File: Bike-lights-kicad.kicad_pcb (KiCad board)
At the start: 2 copper layers, 49 parts, among them J1 tag-connect-swd, Q1 2N7002, Q2 2N7002, Q3 2N7002, Q4 2N7002, Q5 2N7002, SW1 SW_Push, U1 ADP2108AUJ-1.8, U2 MC34673, U3 DIO6605B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

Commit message: output ready
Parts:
- removed R1: 100K, Resistor_SMD:R_0603_1608Metric
- added REF**: MountingHole_3mm, MountingHole:MountingHole_3mm, F.Cu at (52.5, 7.85)
- added REF**: MountingHole_3mm, MountingHole:MountingHole_3mm, F.Cu at (16.5, 7.85)
- added REF**: MountingHole_2.2mm_M2_ISO14580_Pad, MountingHole:MountingHole_2.2mm_M2_ISO14580_Pad, F.Cu at (40.5, 7.85)
- J1, TP1, TP2, TP3, TP4: moved to B.Cu
- moved C9 174.9 mm to (3.60, 2.40)
- moved R4 165.7 mm to (3.60, 13.3)
- moved R8 163.3 mm to (9.70, 11.1)
- moved R9 159.6 mm to (21.7, 11.1)
- moved TP4 153.9 mm to (3.47, 10.5), turned to 90 degrees
- moved Q1 152.3 mm to (10.1, 13.6), turned to 180 degrees
- moved TP3 152.2 mm to (3.47, 5.40), turned to -90 degrees
- moved D1 149.7 mm to (10.5, 9.12), turned to 90 degrees
- moved R10 146.3 mm to (33.7, 11.1)
- moved Q2 144.8 mm to (22.1, 13.6), turned to 180 degrees
- moved SW1 142.1 mm to (3.50, 7.85), turned to 90 degrees
- moved D2 137.9 mm to (22.5, 9.12), turned to 90 degrees
- moved Q3 134.6 mm to (34.1, 13.6), turned to 180 degrees
- moved R11 132.8 mm to (45.7, 11.1)
- moved R12 129.9 mm to (57.7, 11.1)
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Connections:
- C7 pad 1: /VBATT -> /VBAT
- TP1 pad 1: /VBATT -> /VBAT
- U2 pad 4: Net-(R1-Pad1) -> /PM_CHG_5V_INPUT
- U3 pad 7: (no net) -> +5V
- U3 pad 8: +5V -> unconnected-(U3-Pad8)
- U5 pad 2: /VBATT -> /VBAT
- U5 pad 3: /VBATT -> /VBAT
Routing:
- net +1V8: track 0.00 -> 151.0 mm, vias 0 -> 5
- net /PM_CHG_5V_INPUT: track 0.00 -> 108.7 mm, vias 0 -> 6
- net +5V: track 0.00 -> 103.1 mm, vias 0 -> 1
- net /TUBE_BTN: track 0.00 -> 83.2 mm, vias 0 -> 2
- net /D_EN0: track 0.00 -> 64.1 mm, vias 0 -> 2
- net /D_EN1: track 0.00 -> 53.0 mm, vias 0 -> 2
- net /FUEL_INT: track 0.00 -> 47.1 mm, vias 0 -> 2
- net /I2C1_SCL: track 0.00 -> 46.1 mm, vias 0 -> 4
- net /VBAT: track 0.00 -> 45.5 mm, vias 0 -> 5
- net /I2C1_SDA: track 0.00 -> 44.5 mm, vias 0 -> 2
- net /D_EN2: track 0.00 -> 41.8 mm, vias 0 -> 2
- net GND: track 0.00 -> 34.9 mm, vias 0 -> 44
- net /D_EN3: track 0.00 -> 30.5 mm, vias 0 -> 2
- net /ACC_INT1: track 0.00 -> 29.1 mm
- net /D_EN4: track 0.00 -> 25.6 mm
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- added copper zone on B.Cu, net GND
- added copper zone on F.Cu, net GND
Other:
- board outline added: 105.9 x 15.7 mm
- board text added: "5V"
- board text added: "BAT+"
- board text added: "BAT-"
- board text added: "CHG INPUT"
- board text added: "GND"
- board text added: "TO BATTERY max 1A charge"
- board text added: "bikelight rev B Alexis Marquet"

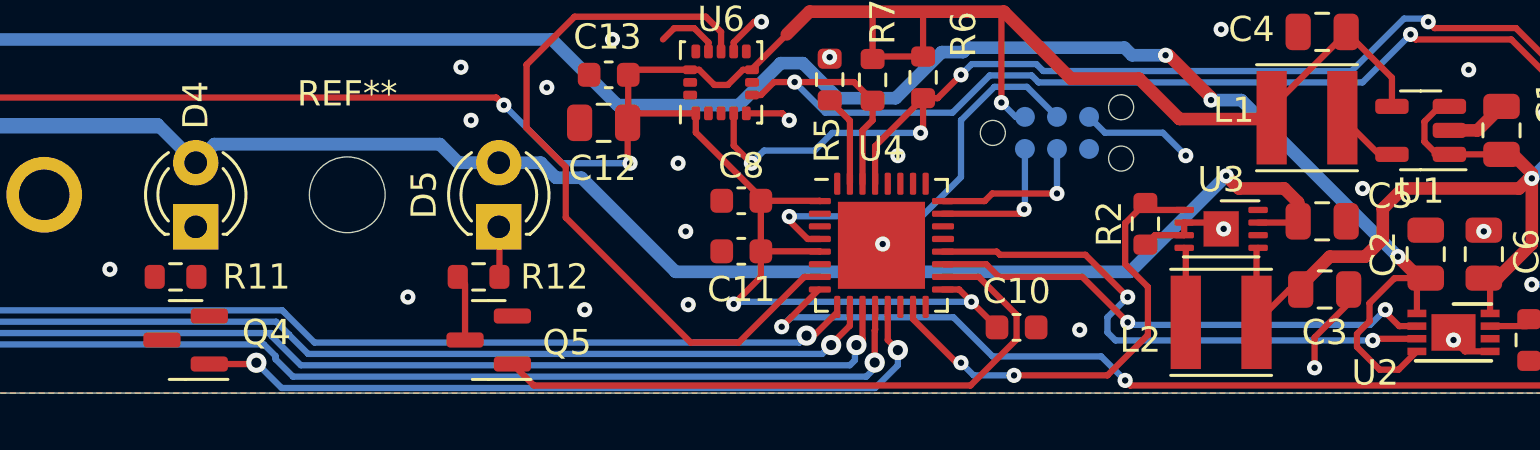
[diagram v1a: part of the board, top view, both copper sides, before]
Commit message: fixed 3 unconnected nets after sending to production...
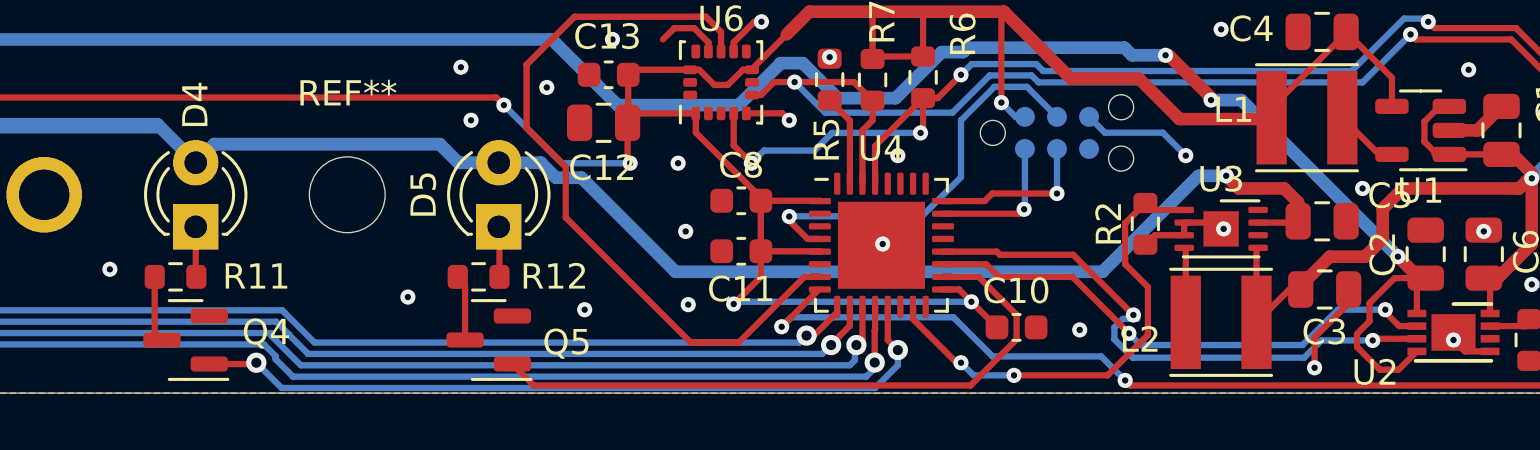
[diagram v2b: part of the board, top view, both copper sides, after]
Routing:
- net Net-(Q4-Pad3): track 0.00 -> 2.62 mm
- net Net-(D4-Pad1): track 0.00 -> 1.99 mm
- net /PM_CHG_CHARGING: track 22.2 -> 22.9 mm
- net /PM_CHG_PRESENT: track 20.3 -> 21.0 mm
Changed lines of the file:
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@@
   (segment (start 88.5625 8.95) (end 90.1 8.95) (width 0.25) (layer "F.Cu") (net 5))
   (via (at 87.3 7.1) (size 0.6) (drill 0.25) (layers "F.Cu" "B.Cu") (net 5))
-  (segment (start 60.166828 6.58) (end 60.761828 7.175) (width 0.5) (layer "B.Cu") (net 5))
+  (segment (start 60.761828 7.175) (end 61.775 7.175) (width 0.5) (layer "B.Cu") (net 5))
   (segment (start 10.5 6.58) (end 12.437062 4.642938) (width 0.508) (layer "B.Cu") (net 5))
   (segment (start 12.437062 4.642938) (end 20.562938 4.642938) (width 0.508) (layer "B.Cu") (net 5))
-  (segment (start 83.5 10.9) (end 87.3 7.1) (width 0.5) (layer "B.Cu") (net 5))
   (segment (start 34.5 6.58) (end 36.016524 5.063476) (width 0.508) (layer "B.Cu") (net 5))
+  (segment (start 82.4 10.9) (end 86.2 7.1) (width 0.5) (layer "B.Cu") (net 5))
   (segment (start 46.5 6.58) (end 47.234001 5.845999) (width 0.508) (layer "B.Cu") (net 5))
   (segment (start 47.234001 5.845999) (end 56.164169 5.845999) (width 0.508) (layer "B.Cu") (net 5))
   (segment (start 34.5 6.58) (end 35.780657 5.299343) (width 0.25) (layer "B.Cu") (net 5))
   (segment (start 61.775 7.175) (end 65.5 10.9) (width 0.5) (layer "B.Cu") (net 5))
-  (segment (start 58.5 6.58) (end 60.166828 6.58) (width 0.5) (layer "B.Cu") (net 5))
+  (segment (start 86.2 7.1) (end 87.3 7.1) (width 0.5) (layer "B.Cu") (net 5))
   (segment (start 46.5 6.58) (end 47.105001 5.974999) (width 0.25) (layer "B.Cu") (net 5))
   (segment (start 45.219343 5.299343) (end 46.5 6.58) (width 0.25) (layer "B.Cu") (net 5))
+  (segment (start 60.166828 6.58) (end 60.761828 7.175) (width 0.5) (layer "B.Cu") (net 5))
   (segment (start 35.780657 5.299343) (end 45.219343 5.299343) (width 0.25) (layer "B.Cu") (net 5))
-  (segment (start 60.761828 7.175) (end 61.775 7.175) (width 0.5) (layer "B.Cu") (net 5))
+  (segment (start 65.5 10.9) (end 82.4 10.9) (width 0.5) (layer "B.Cu") (net 5))
   (segment (start 56.164169 5.845999) (end 56.89817 6.58) (width 0.508) (layer "B.Cu") (net 5))
   (segment (start 56.89817 6.58) (end 58.5 6.58) (width 0.508) (layer "B.Cu") (net 5))
+  (segment (start 58.5 6.58) (end 60.166828 6.58) (width 0.5) (layer "B.Cu") (net 5))
   (segment (start 36.016524 5.063476) (end 44.983476 5.063476) (width 0.508) (layer "B.Cu") (net 5))
-  (segment (start 65.5 10.9) (end 83.5 10.9) (width 0.5) (layer "B.Cu") (net 5))
   (segment (start 20.562938 4.642938) (end 22.5 6.58) (width 0.508) (layer "B.Cu") (net 5))
   (segment (start 22.5 6.58) (end 34.5 6.58) (width 0.508) (layer "B.Cu") (net 5))
@@
   (segment (start 22.525 11.1) (end 22.525 9.145) (width 0.25) (layer "F.Cu") (net 9))
   (segment (start 34.5 9.12) (end 34.5 11.075) (width 0.25) (layer "F.Cu") (net 10))
+  (segment (start 46.5 11.075) (end 46.525 11.1) (width 0.25) (layer "F.Cu") (net 11))
+  (segment (start 46.5 9.12) (end 46.5 11.075) (width 0.25) (layer "F.Cu") (net 11))
   (segment (start 58.525 11.1) (end 58.525 9.145) (width 0.25) (layer "F.Cu") (net 12))
   (segment (start 79.1245 8.6) (end 76.0875 8.6) (width 0.25) (layer "F.Cu") (net 13))
@@
   (segment (start 49.9 15.5) (end 48.9 14.5) (width 0.25) (layer "B.Cu") (net 25))
   (segment (start 74.3 14.6) (end 73.4 15.5) (width 0.25) (layer "B.Cu") (net 25))
+  (segment (start 44.875 13.3125) (end 45.1625 13.6) (width 0.25) (layer "F.Cu") (net 26))
+  (segment (start 44.875 11.1) (end 44.875 13.3125) (width 0.25) (layer "F.Cu") (net 26))
   (segment (start 79 13.577817) (end 79 12.6) (width 0.25) (layer "F.Cu") (net 27))
   (segment (start 77.5 11.1) (end 76.0875 11.1) (width 0.25) (layer "F.Cu") (net 27))
@@
   (segment (start 71.425 4.6) (end 70.2125 3.3875) (width 0.25) (layer "B.Cu") (net 33))
   (segment (start 77.938604 3.125) (end 76.463604 4.6) (width 0.25) (layer "B.Cu") (net 33))
+  (segment (start 77.8 10.6) (end 76.0875 10.6) (width 0.25) (layer "F.Cu") (net 34))
   (segment (start 93.6 12.4) (end 93.6 12.5) (width 0.25) (layer "F.Cu") (net 34))
-  (segment (start 77.8 10.6) (end 76.0875 10.6) (width 0.25) (layer "F.Cu") (net 34))
   (segment (start 93.6 12.5) (end 94.15 13.05) (width 0.25) (layer "F.Cu") (net 34))
   (segment (start 94.15 13.05) (end 94.85 13.05) (width 0.25) (layer "F.Cu") (net 34))
-  (segment (start 83.4 12.9) (end 81.6 11.1) (width 0.25) (layer "F.Cu") (net 34))
-  (segment (start 81.6 11.1) (end 78.3 11.1) (width 0.25) (layer "F.Cu") (net 34))
+  (segment (start 81.212466 11.1) (end 78.3 11.1) (width 0.25) (layer "F.Cu") (net 34))
+  (segment (start 83.45 13.337534) (end 81.212466 11.1) (width 0.25) (layer "F.Cu") (net 34))
   (segment (start 78.3 11.1) (end 77.8 10.6) (width 0.25) (layer "F.Cu") (net 34))
   (via (at 93.6 12.4) (size 0.6) (drill 0.25) (layers "F.Cu" "B.Cu") (net 34))
-  (via (at 83.4 12.9) (size 0.6) (drill 0.25) (layers "F.Cu" "B.Cu") (net 34))
-  (segment (start 93 13) (end 93.6 12.4) (width 0.25) (layer "B.Cu") (net 34))
-  (segment (start 83.5 13) (end 93 13) (width 0.25) (layer "B.Cu") (net 34))
-  (segment (start 83.4 12.9) (end 83.5 13) (width 0.25) (layer "B.Cu") (net 34))
-  (segment (start 81.725 10.225) (end 78.341116 10.225) (width 0.25) (layer "F.Cu") (net 35))
+  (via (at 83.45 13.337534) (size 0.6) (drill 0.25) (layers "F.Cu" "B.Cu") (net 34))
+  (segment (start 91.721141 12.4) (end 93.6 12.4) (width 0.25) (layer "B.Cu") (net 34))
+  (segment (start 83.45 13.337534) (end 83.912466 13.8) (width 0.25) (layer "B.Cu") (net 34))
+  (segment (start 90.321141 13.8) (end 91.721141 12.4) (width 0.25) (layer "B.Cu") (net 34))
+  (segment (start 83.912466 13.8) (end 90.321141 13.8) (width 0.25) (layer "B.Cu") (net 34))
   (segment (start 78.341116 10.225) (end 78.216116 10.1) (width 0.25) (layer "F.Cu") (net 35))
+  (segment (start 78.216116 10.1) (end 76.0875 10.1) (width 0.25) (layer "F.Cu") (net 35))
+  (segment (start 83.6255 12.608868) (end 81.241632 10.225) (width 0.25) (layer "F.Cu") (net 35))
   (segment (start 93.168671 13.55) (end 93.102667 13.616004) (width 0.25) (layer "F.Cu") (net 35))
-  (segment (start 83.4 11.9) (end 81.725 10.225) (width 0.25) (layer "F.Cu") (net 35))
   (segment (start 94.85 13.55) (end 93.168671 13.55) (width 0.25) (layer "F.Cu") (net 35))
-  (segment (start 78.216116 10.1) (end 76.0875 10.1) (width 0.25) (layer "F.Cu") (net 35))
-  (via (at 83.4 11.9) (size 0.6) (drill 0.25) (layers "F.Cu" "B.Cu") (net 35))
+  (segment (start 81.241632 10.225) (end 78.341116 10.225) (width 0.25) (layer "F.Cu") (net 35))
+  (via (at 83.6255 12.608868) (size 0.6) (drill 0.25) (layers "F.Cu" "B.Cu") (net 35))
   (via (at 93.102667 13.616004) (size 0.6) (drill 0.25) (layers "F.Cu" "B.Cu") (net 35))
-  (segment (start 82.6 13.3) (end 82.916004 13.616004) (width 0.25) (layer "B.Cu") (net 35))
-  (segment (start 82.6 12.7) (end 82.6 13.3) (width 0.25) (layer "B.Cu") (net 35))
-  (segment (start 82.916004 13.616004) (end 93.102667 13.616004) (width 0.25) (layer "B.Cu") (net 35))
-  (segment (start 83.4 11.9) (end 82.6 12.7) (width 0.25) (layer "B.Cu") (net 35))
+  (segment (start 82.875 13.099361) (end 82.875 13.575707) (width 0.25) (layer "B.Cu") (net 35))
+  (segment (start 83.211827 12.762534) (end 82.875 13.099361) (width 0.25) (layer "B.Cu") (net 35))
+  (segment (start 91.070823 13.616004) (end 93.102667 13.616004) (width 0.25) (layer "B.Cu") (net 35))
+  (segment (start 83.599293 14.3) (end 90.386827 14.3) (width 0.25) (layer "B.Cu") (net 35))
+  (segment (start 83.6255 12.608868) (end 83.779166 12.762534) (width 0.25) (layer "B.Cu") (net 35))
+  (segment (start 90.386827 14.3) (end 91.070823 13.616004) (width 0.25) (layer "B.Cu") (net 35))
+  (segment (start 82.875 13.575707) (end 83.599293 14.3) (width 0.25) (layer "B.Cu") (net 35))
+  (segment (start 83.779166 12.762534) (end 83.211827 12.762534) (width 0.25) (layer "B.Cu") (net 35))
   (segment (start 71.2125 11.1) (end 70.6 11.1) (width 0.25) (layer "F.Cu") (net 41))
   (segment (start 68 13.7) (end 66.1 13.7) (width 0.25) (layer "F.Cu") (net 41))
